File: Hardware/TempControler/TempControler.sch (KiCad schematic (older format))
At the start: 0 parts

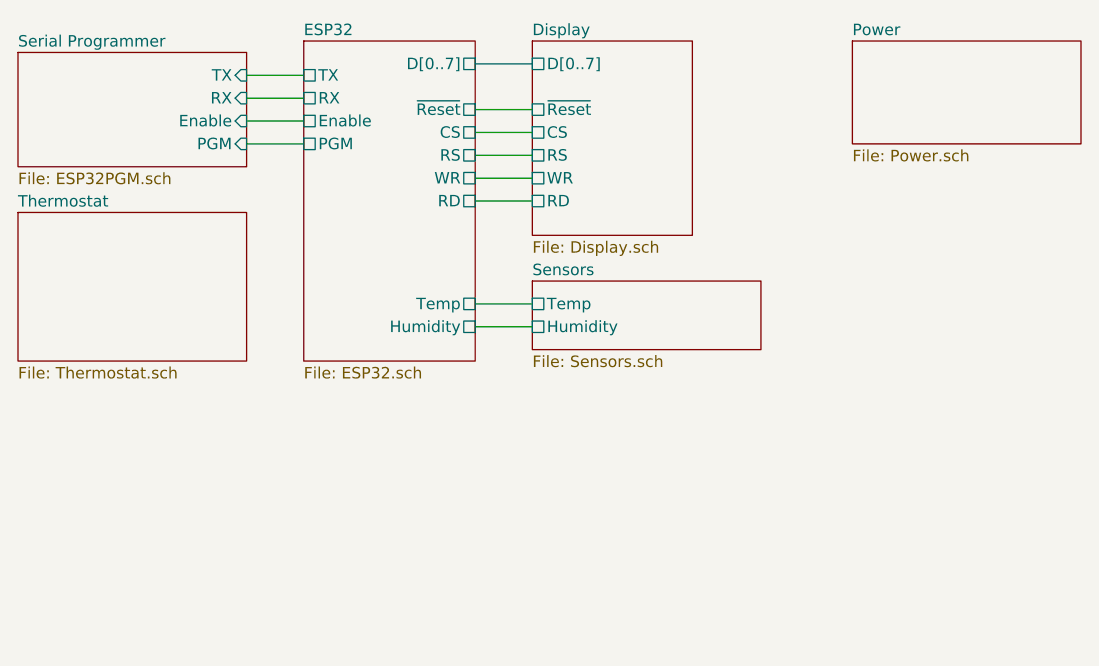
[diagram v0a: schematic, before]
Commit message: Schematic Complete
DRC - Done
Schematic - Done
Values - Done
Part Selection - In Progress
Footprint assignment- In Progress
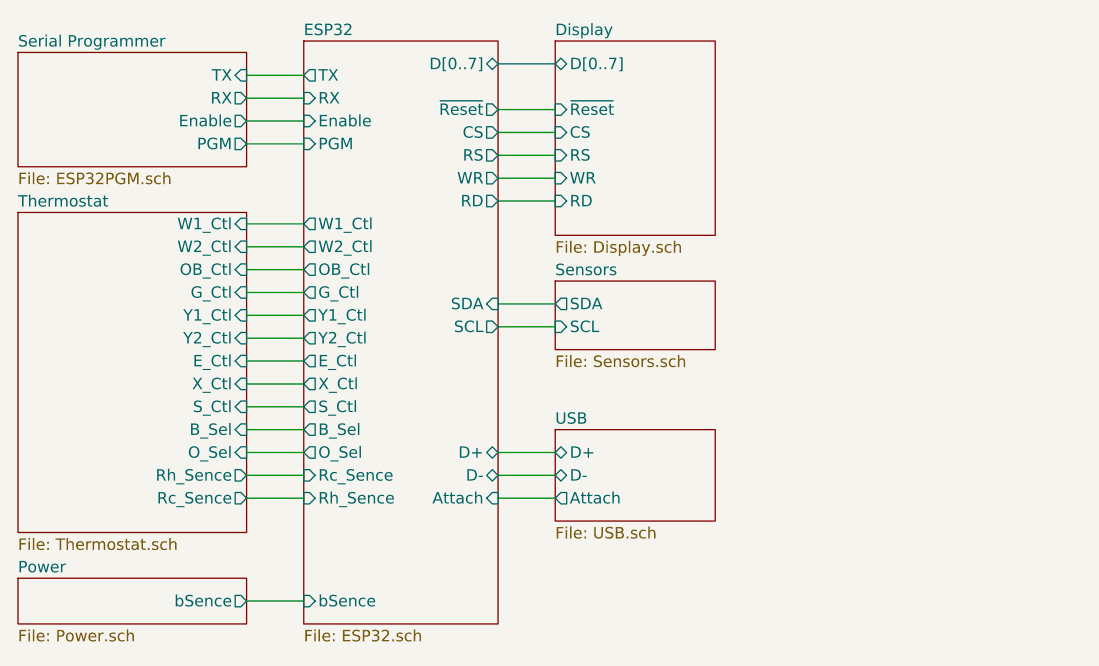
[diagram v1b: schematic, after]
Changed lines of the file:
@@
 $Descr USLetter 11000 8500
 encoding utf-8
-Sheet 1 7
+Sheet 1 8
 Title "TempControler"
 Date ""
@@
 $EndDescr
 $Sheet
-S 2050 1400 750  1400
+S 2050 1400 850  2550
 U 62D47889
 F0 "ESP32" 50
 F1 "ESP32.sch" 50
-F2 "D[0..7]" U R 2800 1500 50
-F3 "~Reset" U R 2800 1700 50
-F4 "CS" U R 2800 1800 50
-F5 "RS" U R 2800 1900 50
-F6 "WR" U R 2800 2000 50
-F7 "RD" U R 2800 2100 50
-F8 "Temp" U R 2800 2550 50
-F9 "Humidity" U R 2800 2650 50
-F10 "Enable" U L 2050 1750 50
-F11 "TX" U L 2050 1550 50
-F12 "RX" U L 2050 1650 50
-F13 "PGM" U L 2050 1850 50
+F2 "D[0..7]" T R 2900 1500 50
+F3 "~Reset" O R 2900 1700 50
+F4 "CS" O R 2900 1800 50
+F5 "RS" O R 2900 1900 50
+F6 "WR" O R 2900 2000 50
+F7 "RD" O R 2900 2100 50
+F8 "Enable" I L 2050 1750 50
+F9 "TX" O L 2050 1550 50
+F10 "RX" I L 2050 1650 50
+F11 "PGM" I L 2050 1850 50
+F12 "D+" T R 2900 3200 50
+F13 "D-" T R 2900 3300 50
+F14 "W1_Ctl" O L 2050 2200 50
+F15 "W2_Ctl" O L 2050 2300 50
+F16 "OB_Ctl" O L 2050 2400 50
+F17 "G_Ctl" O L 2050 2500 50
+F18 "Y1_Ctl" O L 2050 2600 50
+F19 "Y2_Ctl" O L 2050 2700 50
+F20 "E_Ctl" O L 2050 2800 50
+F21 "X_Ctl" O L 2050 2900 50
+F22 "S_Ctl" O L 2050 3000 50
+F23 "B_Sel" O L 2050 3100 50
+F24 "O_Sel" O L 2050 3200 50
+F25 "Rc_Sence" I L 2050 3300 50
+F26 "Rh_Sence" I L 2050 3400 50
+F27 "Attach" I R 2900 3400 50
+F28 "bSence" I L 2050 3850 50
+F29 "SDA" I R 2900 2550 50
+F30 "SCL" O R 2900 2650 50
 $EndSheet
 $Sheet
-S 3050 1400 700  850
+S 3150 1400 700  850
 U 62D4790F
 F0 "Display" 50
 F1 "Display.sch" 50
-F2 "D[0..7]" U L 3050 1500 50
-F3 "~Reset" U L 3050 1700 50
-F4 "CS" U L 3050 1800 50
-F5 "RS" U L 3050 1900 50
-F6 "WR" U L 3050 2000 50
-F7 "RD" U L 3050 2100 50
+F2 "D[0..7]" T L 3150 1500 50
+F3 "~Reset" I L 3150 1700 50
+F4 "CS" I L 3150 1800 50
+F5 "RS" I L 3150 1900 50
+F6 "WR" I L 3150 2000 50
+F7 "RD" I L 3150 2100 50
 $EndSheet
 $Sheet
-S 4450 1400 1000 450
+S 800  3750 1000 200
 U 62D479C8
 F0 "Power" 50
 F1 "Power.sch" 50
+F2 "bSence" O R 1800 3850 50
 $EndSheet
 $Sheet
-S 3050 2450 1000 300
+S 3150 2450 700  300
 U 62D47A27
 F0 "Sensors" 50
 F1 "Sensors.sch" 50
-F2 "Temp" U L 3050 2550 50
-F3 "Humidity" U L 3050 2650 50
+F2 "SDA" O L 3150 2550 50
+F3 "SCL" I L 3150 2650 50
 $EndSheet
 $Sheet
@@
 F1 "ESP32PGM.sch" 50
 F2 "TX" I R 1800 1550 50
-F3 "RX" I R 1800 1650 50
-F4 "Enable" I R 1800 1750 50
-F5 "PGM" I R 1800 1850 50
+F3 "RX" O R 1800 1650 50
+F4 "Enable" O R 1800 1750 50
+F5 "PGM" O R 1800 1850 50
 $EndSheet
 Wire Wire Line
-	2800 1700 3050 1700
+	2900 1700 3150 1700
 Wire Bus Line
-	2800 1500 3050 1500
+	2900 1500 3150 1500
 Wire Wire Line
-	2800 1800 3050 1800
+	2900 1800 3150 1800
 Wire Wire Line
-	2800 1900 3050 1900
+	2900 1900 3150 1900
 Wire Wire Line
-	2800 2000 3050 2000
+	2900 2000 3150 2000
 Wire Wire Line
-	2800 2100 3050 2100
+	2900 2100 3150 2100
 Wire Wire Line
 	1800 1550 2050 1550
@@
 	1800 1850 2050 1850
 Wire Wire Line
-	3050 2550 2800 2550
+	3150 2550 2900 2550
 Wire Wire Line
-	3050 2650 2800 2650
+	3150 2650 2900 2650
 $Sheet
-S 800  2150 1000 650
+S 800  2150 1000 1400
 U 62E5786F
 F0 "Thermostat" 50
 F1 "Thermostat.sch" 50
+F2 "W1_Ctl" I R 1800 2200 50
+F3 "W2_Ctl" I R 1800 2300 50
+F4 "OB_Ctl" I R 1800 2400 50
+F5 "G_Ctl" I R 1800 2500 50
+F6 "Y1_Ctl" I R 1800 2600 50
+F7 "Y2_Ctl" I R 1800 2700 50
+F8 "E_Ctl" I R 1800 2800 50
+F9 "X_Ctl" I R 1800 2900 50
+F10 "S_Ctl" I R 1800 3000 50
+F11 "B_Sel" I R 1800 3100 50
+F12 "O_Sel" I R 1800 3200 50
+F13 "Rh_Sence" O R 1800 3300 50
+F14 "Rc_Sence" O R 1800 3400 50
 $EndSheet
+Wire Wire Line
+	1800 2200 2050 2200
+Wire Wire Line
+	1800 2300 2050 2300
+Wire Wire Line
+	1800 2400 2050 2400
+Wire Wire Line
+	1800 2500 2050 2500
+Wire Wire Line
+	1800 2600 2050 2600
+Wire Wire Line
+	1800 2700 2050 2700
+Wire Wire Line
+	1800 2800 2050 2800
+Wire Wire Line
+	1800 2900 2050 2900
+Wire Wire Line
+	1800 3000 2050 3000
+Wire Wire Line
+	1800 3100 2050 3100
+Wire Wire Line
+	1800 3200 2050 3200
+Wire Wire Line
+	1800 3300 2050 3300
+Wire Wire Line
+	1800 3400 2050 3400
+$Sheet
+S 3150 3100 700  400
+U 63004DA6
+F0 "USB" 50
+F1 "USB.sch" 50
+F2 "D+" T L 3150 3200 50
+F3 "D-" T L 3150 3300 50
+F4 "Attach" O L 3150 3400 50
+$EndSheet
+Wire Wire Line
+	3150 3300 2900 3300
+Wire Wire Line
+	3150 3400 2900 3400
+Wire Wire Line
+	1800 3850 2050 3850
+Wire Wire Line
+	2900 3200 3150 3200
 $EndSCHEMATC
